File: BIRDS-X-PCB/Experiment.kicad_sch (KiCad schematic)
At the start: 19 parts, among them U301 VT01, U302 VT01, U303 VT01, U304 VT01, U305 TL974IPWR, U306 ADG734, U307 LM335DT, U308 LM334M

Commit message: Finish layout
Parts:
- added TP301: TestPoint, TestPoint:TestPoint_Pad_D2.0mm, symbol Connector:TestPoint
- R301: renamed from R303; footprint Resistor_SMD:R_1206_3216Metric_Pad1.30x1.75mm_HandSolder -> Resistor_SMD:R_0805_2012Metric_Pad1.20x1.40mm_HandSolder
- R302: renamed from R2; footprint Resistor_SMD:R_1206_3216Metric -> Resistor_SMD:R_0805_2012Metric_Pad1.20x1.40mm_HandSolder
- R303: renamed from R1; footprint Resistor_SMD:R_1206_3216Metric -> Resistor_SMD:R_0805_2012Metric_Pad1.20x1.40mm_HandSolder
- R304: renamed from R3; footprint Resistor_SMD:R_1206_3216Metric -> Resistor_SMD:R_0805_2012Metric_Pad1.20x1.40mm_HandSolder
- R305: renamed from R4; footprint Resistor_SMD:R_1206_3216Metric -> Resistor_SMD:R_0805_2012Metric_Pad1.20x1.40mm_HandSolder
- R306: renamed from R5; footprint Resistor_SMD:R_1206_3216Metric -> Resistor_SMD:R_0805_2012Metric_Pad1.20x1.40mm_HandSolder
- R307: renamed from R6; footprint Resistor_SMD:R_1206_3216Metric -> Resistor_SMD:R_0805_2012Metric_Pad1.20x1.40mm_HandSolder
- R308: renamed from R7; footprint Resistor_SMD:R_1206_3216Metric -> Resistor_SMD:R_0805_2012Metric_Pad1.20x1.40mm_HandSolder
- R309: renamed from R8; footprint Resistor_SMD:R_1206_3216Metric -> Resistor_SMD:R_0805_2012Metric_Pad1.20x1.40mm_HandSolder
- R310: renamed from R9; footprint Resistor_SMD:R_1206_3216Metric -> Resistor_SMD:R_0805_2012Metric_Pad1.20x1.40mm_HandSolder
- R311: renamed from R10; footprint Resistor_SMD:R_1206_3216Metric -> Resistor_SMD:R_0805_2012Metric_Pad1.20x1.40mm_HandSolder
- U301, U302, U303, U304: value VT01 -> VT03; footprint Package_SO:SO-6_4.4x3.6mm_P1.27mm -> Package_TO_SOT_SMD:SOT-23-6_Handsoldering; symbol BIRDS-X_Symbols_Lib:VT01_Radfet -> BIRDS-X_Symbols_Lib:VT03_Radfet
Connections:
- net +5V is gone; now on net +12V: U308.4
- net GND: no longer U301.3 (GATE_R2), U301.5 (DRAIN_R2), U302.3 (GATE_R2), U302.5 (DRAIN_R2), U303.3 (GATE_R2), U303.5 (DRAIN_R2), U304.3 (GATE_R2), U304.5 (DRAIN_R2)
- net TEMP_SENSE_1: now also TP301.1
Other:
- note added: "Op Amps act as analog voltage buffers"
- note added: "VT03 RADFETs Sense Radiation"
- note removed: "Op Amp act as analog voltage buffers"
- note removed: "TODO confirm 5V is right here Parker thinks maybe it should be 12V or 24V"
- note removed: "VT01 RADFETs Sense Radiation"

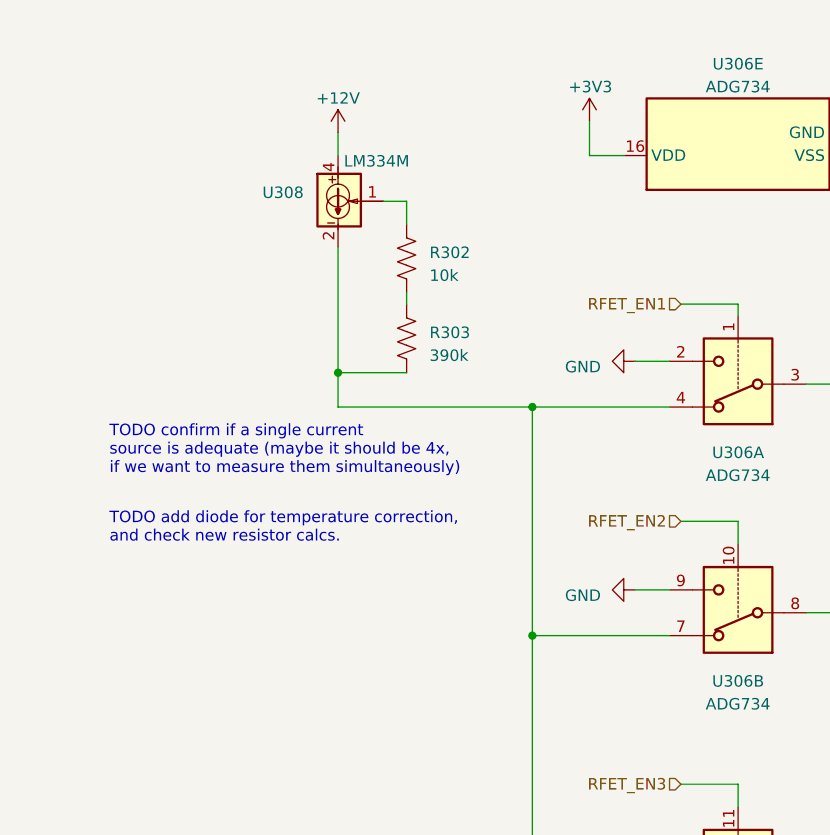
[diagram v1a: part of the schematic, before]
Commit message: Update tempo current source
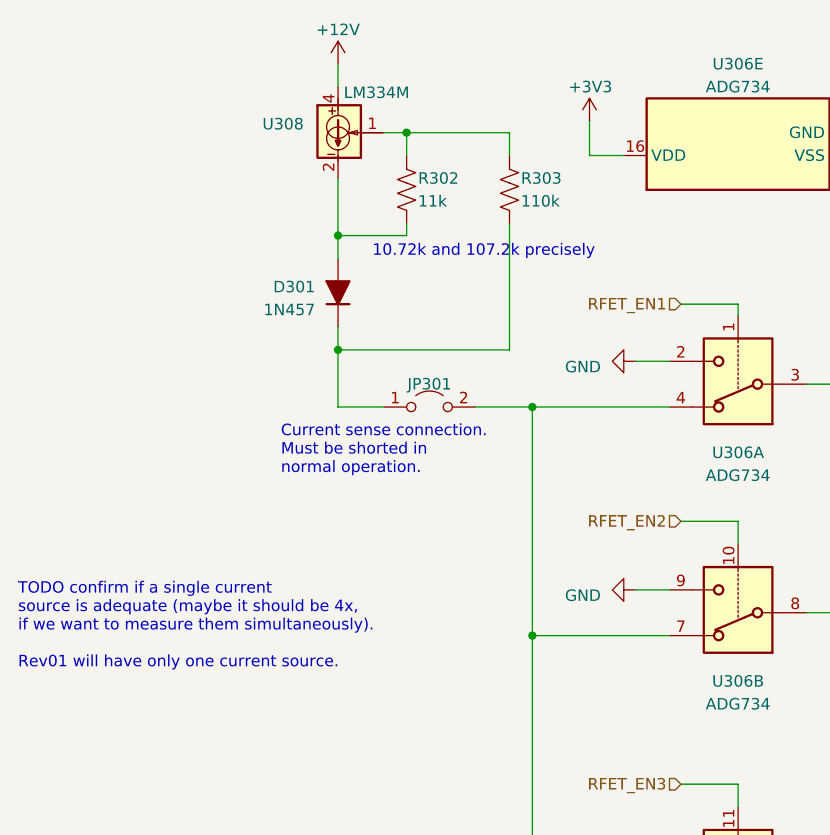
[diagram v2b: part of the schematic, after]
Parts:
- added D301: 1N457, Diode_THT_AKL:D_DO-35_SOD27_P7.62mm_Horizontal, symbol BIRDS-X_Symbols_Lib:1N457
- added JP301: Jumper_2_Open, symbol Jumper:Jumper_2_Open
- R302: value 10k -> 11k
- R303: value 390k -> 110k
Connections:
- net at R302.1, U308.1: now also R303.1
- net at R302.2: now also U308.2, U308.3, U308.6, U308.7, D301.2 (A); no longer R303.1
- new net: JP301.2 (B), U306.14, U306.17, U306.4, U306.7
- new net: D301.1 (K), JP301.1 (A), R303.2
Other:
- note added: "10.72k and 107.2k precisely"
- note added: "Current sense connection. Must be shorted in normal operation."
- note added: "TODO confirm if a single current source is adequate (maybe it should be 4x, if we want to measure them simultaneously). Rev01 will have only one current source."
- note removed: "TODO add diode for temperature correction, and check new resistor calcs."
- note removed: "TODO confirm if a single current source is adequate (maybe it should be 4x, if we want to measure them simultaneously)"
- moved on the sheet: R302, R303, U308

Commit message: Do some routing
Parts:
- D301: footprint Diode_THT_AKL:D_DO-35_SOD27_P7.62mm_Horizontal -> Diode_THT:D_DO-35_SOD27_P7.62mm_Horizontal
- JP301: footprint (none) -> Connector_PinHeader_2.54mm:PinHeader_1x02_P2.54mm_Vertical
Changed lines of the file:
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@@
       (effects (font (size 1.27 1.27)) hide)
     )
-    (property "Footprint" "" (at 64.77 59.69 0)
+    (property "Footprint" "Connector_PinHeader_2.54mm:PinHeader_1x02_P2.54mm_Vertical" (at 64.77 59.69 0)
       (effects (font (size 1.27 1.27)) hide)
     )
@@
       (effects (font (size 1.27 1.27)) (justify left))
     )
-    (property "Footprint" "Diode_THT_AKL:D_DO-35_SOD27_P7.62mm_Horizontal" (at 54.61 46.99 0)
-      (effects (font (size 1.27 1.27)) hide)
-    )
+    (property "Footprint" "Diode_THT:D_DO-35_SOD27_P7.62mm_Horizontal" (at 54.61 46.99 0)
+      (effects (font (size 1.27 1.27)) hide)
+    )

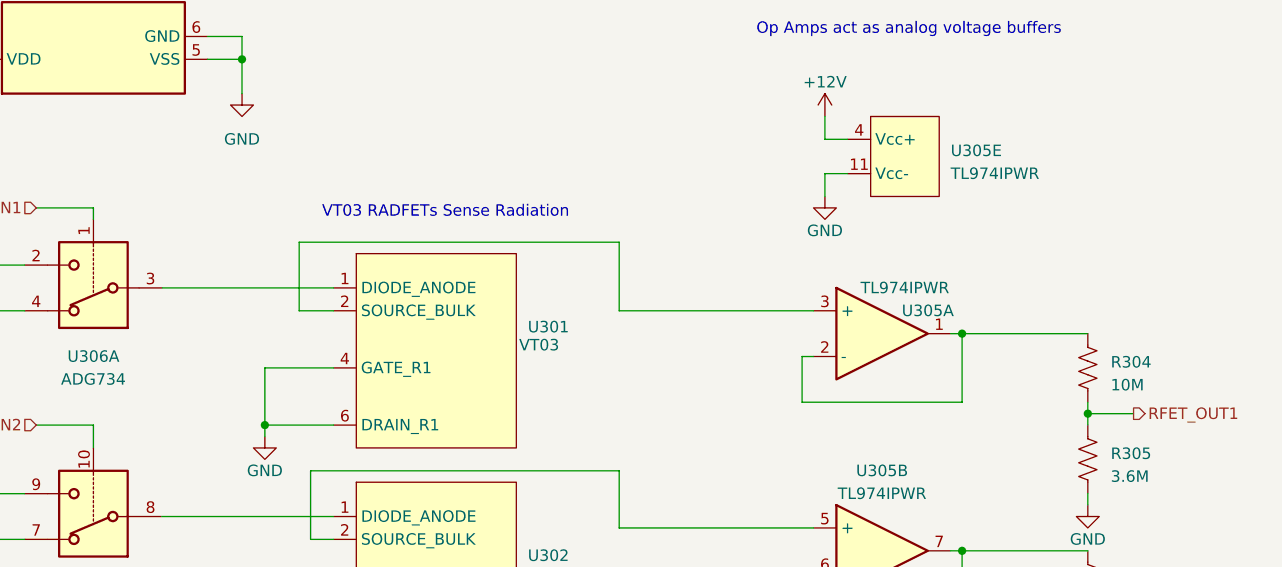
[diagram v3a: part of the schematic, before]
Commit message: Minor layout changes to consolodate ground planes
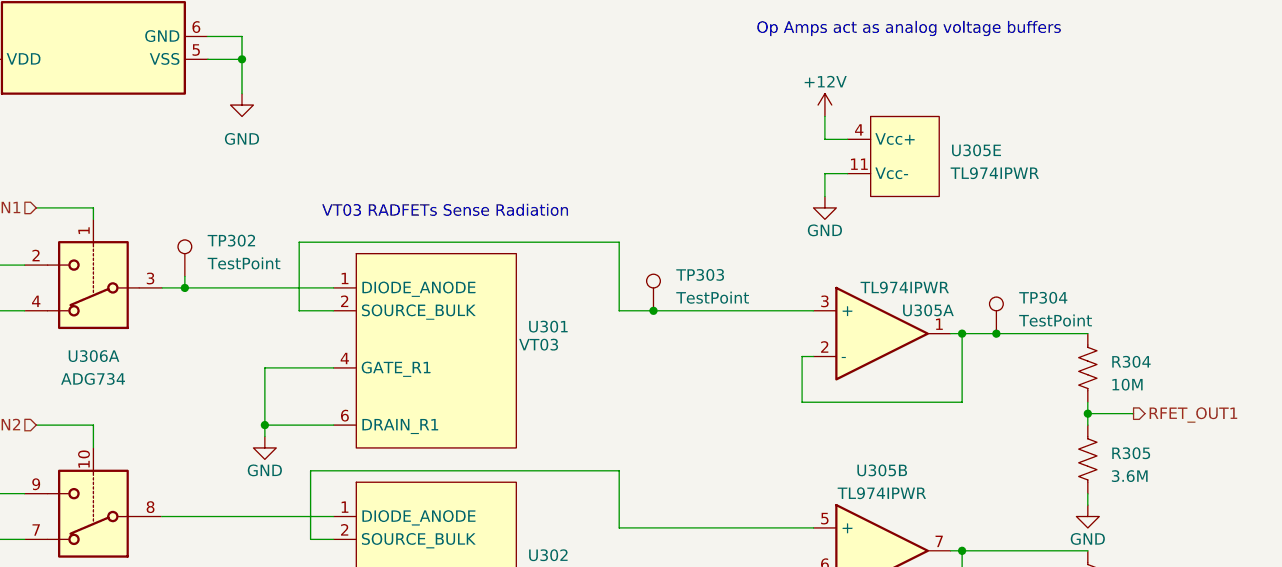
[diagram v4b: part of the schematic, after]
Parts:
- added TP302, TP303, TP304: TestPoint, symbol Connector:TestPoint
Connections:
- net at R304.1, U305.1, U305.2 (-): now also TP304.1
- net at U301.2 (SOURCE_BULK), U305.3 (+): now also TP303.1
- net at U301.1 (DIODE_ANODE), U306.3: now also TP302.1
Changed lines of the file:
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@@
   (junction (at 62.23 29.21) (diameter 0) (color 0 0 0 0)
   )
+  (junction (at 161.29 59.69) (diameter 0) (color 0 0 0 0)
+  )
+  (junction (at 199.39 62.23) (diameter 0) (color 0 0 0 0)
+  )
   (junction (at 195.58 86.36) (diameter 0) (color 0 0 0 0)
   )
+  (junction (at 109.22 57.15) (diameter 0) (color 0 0 0 0)
+  )
   (junction (at 209.55 95.25) (diameter 0) (color 0 0 0 0)
   )
@@
   )
   (no_connect (at 41.91 181.61))
+  (wire (pts (xy 161.29 59.69) (xy 179.07 59.69))
+    (stroke (width 0) (type default))
+  )
   (wire (pts (xy 54.61 53.34) (xy 54.61 59.69))
     (stroke (width 0) (type default))
@@
     (stroke (width 0) (type default))
   )
+  (wire (pts (xy 199.39 62.23) (xy 209.55 62.23))
+    (stroke (width 0) (type default))
+  )
   (wire (pts (xy 111.76 29.21) (xy 115.57 29.21))
     (stroke (width 0) (type default))
@@
     (stroke (width 0) (type default))
   )
+  (wire (pts (xy 109.22 57.15) (xy 125.73 57.15))
+    (stroke (width 0) (type default))
+  )
   (wire (pts (xy 54.61 53.34) (xy 73.66 53.34))
     (stroke (width 0) (type default))
@@
     (stroke (width 0) (type default))
   )
-  (wire (pts (xy 157.48 59.69) (xy 179.07 59.69))
+  (wire (pts (xy 157.48 59.69) (xy 161.29 59.69))
     (stroke (width 0) (type default))
   )
@@
     (stroke (width 0) (type default))
   )
-  (wire (pts (xy 195.58 62.23) (xy 209.55 62.23))
+  (wire (pts (xy 195.58 62.23) (xy 199.39 62.23))
     (stroke (width 0) (type default))
   )
@@
     (stroke (width 0) (type default))
   )
-  (wire (pts (xy 106.68 57.15) (xy 125.73 57.15))
+  (wire (pts (xy 106.68 57.15) (xy 109.22 57.15))
     (stroke (width 0) (type default))
   )
@@
   )
   (wire (pts (xy 121.92 59.69) (xy 125.73 59.69))
+    (stroke (width 0) (type default))
+  )
+  (wire (pts (xy 109.22 55.88) (xy 109.22 57.15))
     (stroke (width 0) (type default))
   )
@@
     )
   )
+  (symbol (lib_id "Connector:TestPoint") (at 109.22 55.88 0) (unit 1)
+    (in_bom yes) (on_board yes) (dnp no) (fields_autoplaced)
+    (property "Reference" "TP302" (at 111.76 51.943 0)
+      (effects (font (size 1.27 1.27)) (justify left))
+    )
+    (property "Value" "TestPoint" (at 111.76 54.483 0)
+      (effects (font (size 1.27 1.27)) (justify left))
+    )
+    (property "Footprint" "" (at 114.3 55.88 0)
+      (effects (font (size 1.27 1.27)) hide)
+    )
+    (property "Datasheet" "~" (at 114.3 55.88 0)
+      (effects (font (size 1.27 1.27)) hide)
+    )
+    (pin "1")
+    (instances
+      (project "BIRDS-X-PCB"
+        (path "/c2796b15-795a-4d6e-ad4b-0ba87ded4bc9/adc73a10-1d27-484e-8ce9-d638694b8e29"
+          (reference "TP302") (unit 1)
+        )
+      )
+    )
+  )
   (symbol (lib_id "power:GND") (at 87.63 109.22 270) (unit 1)
     (in_bom yes) (on_board yes) (dnp no) (fields_autoplaced)
@@
         (path "/c2796b15-795a-4d6e-ad4b-0ba87ded4bc9/adc73a10-1d27-484e-8ce9-d638694b8e29"
           (reference "R306") (unit 1)
+        )
+      )
+    )
+  )
+  (symbol (lib_id "Connector:TestPoint") (at 199.39 62.23 0) (unit 1)
+    (in_bom yes) (on_board yes) (dnp no) (fields_autoplaced)
+    (property "Reference" "TP304" (at 201.93 58.293 0)
+      (effects (font (size 1.27 1.27)) (justify left))
+    )
+    (property "Value" "TestPoint" (at 201.93 60.833 0)
+      (effects (font (size 1.27 1.27)) (justify left))
+    )
+    (property "Footprint" "" (at 204.47 62.23 0)
+      (effects (font (size 1.27 1.27)) hide)
+    )
+    (property "Datasheet" "~" (at 204.47 62.23 0)
+      (effects (font (size 1.27 1.27)) hide)
+    )
+    (pin "1")
+    (instances
+      (project "BIRDS-X-PCB"
+        (path "/c2796b15-795a-4d6e-ad4b-0ba87ded4bc9/adc73a10-1d27-484e-8ce9-d638694b8e29"
+          (reference "TP304") (unit 1)
         )
       )
@@
         )
       )
+    )
+  )
+  (symbol (lib_id "Connector:TestPoint") (at 161.29 59.69 0) (unit 1)
+    (in_bom yes) (on_board yes) (dnp no) (fields_autoplaced)
+    (property "Reference" "TP303" (at 163.83 55.753 0)
+      (effects (font (size 1.27 1.27)) (justify left))
+    )
+    (property "Value" "TestPoint" (at 163.83 58.293 0)
+      (effects (font (size 1.27 1.27)) (justify left))
+    )
+    (property "Footprint" "" (at 166.37 59.69 0)
+      (effects (font (size 1.27 1.27)) hide)
+    )
+    (property "Datasheet" "~" (at 166.37 59.69 0)
+      (effects (font (size 1.27 1.27)) hide)
+    )
+    (pin "1")
+    (instances
+      (project "BIRDS-X-PCB"
+        (path "/c2796b15-795a-4d6e-ad4b-0ba87ded4bc9/adc73a10-1d27-484e-8ce9-d638694b8e29"
+          (reference "TP303") (unit 1)
+        )
+      )

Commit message: Add silkscreen labels
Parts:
- TP302, TP303, TP304: footprint (none) -> TestPoint:TestPoint_Pad_D2.0mm
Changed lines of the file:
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@@
       (effects (font (size 1.27 1.27)) (justify left))
     )
-    (property "Footprint" "" (at 114.3 55.88 0)
+    (property "Footprint" "TestPoint:TestPoint_Pad_D2.0mm" (at 114.3 55.88 0)
       (effects (font (size 1.27 1.27)) hide)
     )
@@
       (effects (font (size 1.27 1.27)) (justify left))
     )
-    (property "Footprint" "" (at 204.47 62.23 0)
+    (property "Footprint" "TestPoint:TestPoint_Pad_D2.0mm" (at 204.47 62.23 0)
       (effects (font (size 1.27 1.27)) hide)
     )
@@
       (effects (font (size 1.27 1.27)) (justify left))
     )
-    (property "Footprint" "" (at 166.37 59.69 0)
-      (effects (font (size 1.27 1.27)) hide)
-    )
+    (property "Footprint" "TestPoint:TestPoint_Pad_D2.0mm" (at 166.37 59.69 0)
+      (effects (font (size 1.27 1.27)) hide)
+    )
